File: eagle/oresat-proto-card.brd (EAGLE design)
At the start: 99.8 x 94.7 mm, 120 parts, among them J1 J-SAMTEC-TFM-110-X1-XXX-D-RA, J2 U.FL, J3 U.FL, J4 U.FL, J6 J-SAMTEC-TFM-120-X1-XXX-D-RA, J7 ORESAT-DEBUG-CONNECTOR-SOLAR, Q10 DMP2240UDM, Q2 MOSFET-PCH-SOT23-6, Q7 MOSFET-PCH-SOT23-6, Q8 PMV45EN, Q9 PMV45EN, U1 TCAN330, U10 TPS62111RSA, U11 MIC842LYC5, U12 MIC842LYC5, U2 MAX7310ATE, U6 MAX4211FETE, U7 STM32F091C, X2 16MHZ-2.5x2mm

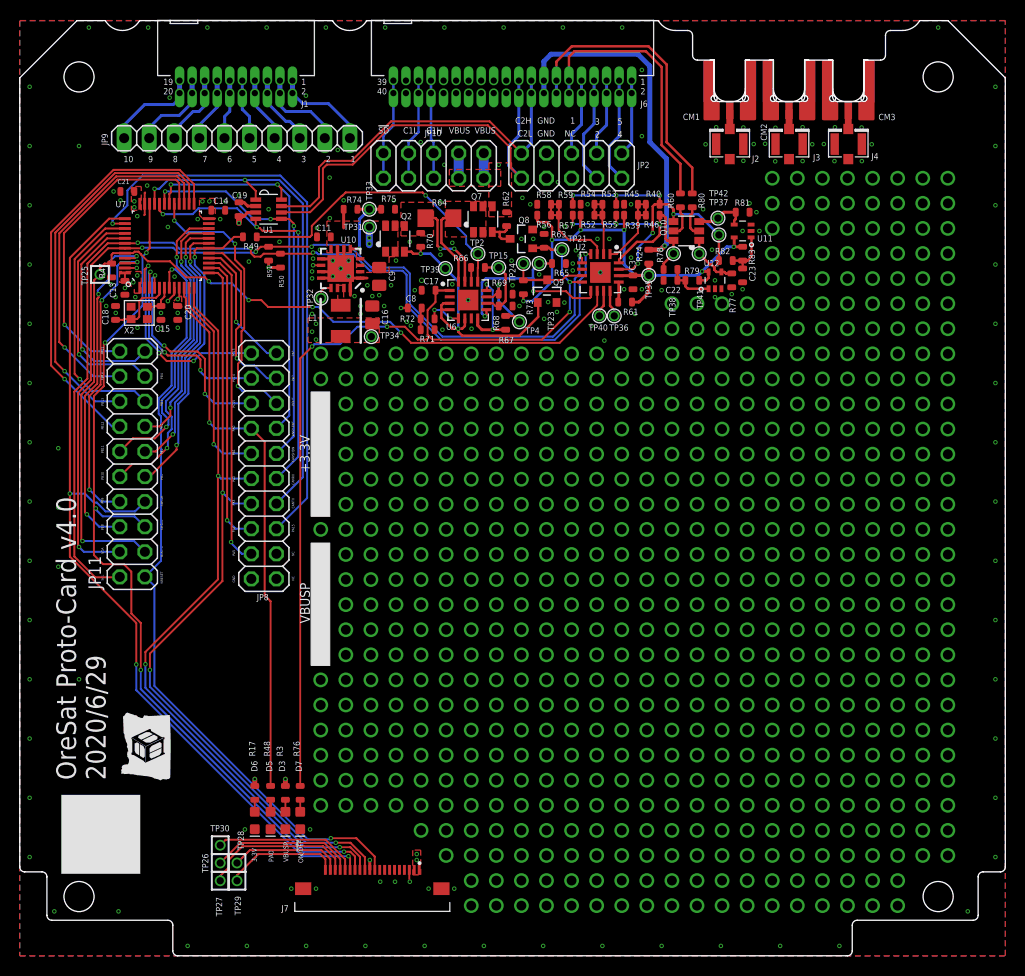
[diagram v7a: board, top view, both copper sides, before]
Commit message: Updated to 4.1: switched to better debug connector, fixed OPD capacitance problem.
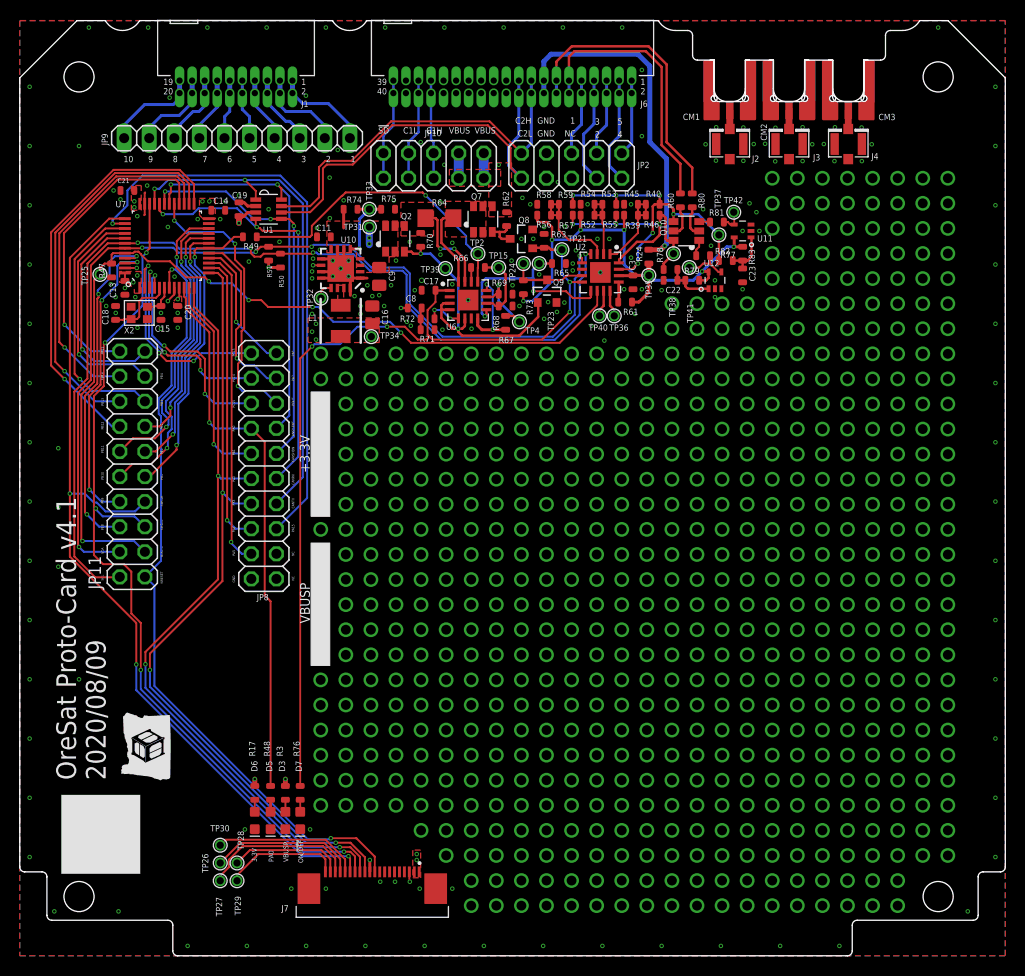
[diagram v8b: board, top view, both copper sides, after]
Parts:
- J7: value ORESAT-DEBUG-CONNECTOR-SOLAR -> ORESAT-DEBUG-CONNECTOR-ALL; device oresat-debug-connector:WURTH_687120183622 -> oresat-debug-connector:TE_2-1734592-0
- R77, R81: value 10k -> 665k
- TP25, TP26, TP27, TP28, TP29, TP30: value TEST-POINT -> TEST-POINT-LARGE-SQUARE; device Tova:2MM-TEST-POINT -> oresat-misc:1X01
- moved R77 3.83 mm to (69.2, 70.9), turned to 180 degrees
- moved R81 2.79 mm to (70.6, 74.3)
- moved TP41 1.72 mm to (67.8, 69.7)
- moved TP42 1.71 mm to (72.3, 75.3)
- moved C21 0.10 mm to (10.9, 77.5)
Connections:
- new net N$398: Q10.1, R77.2
- new net N$400: Q10.3, R81.2
- net GND: no longer R77.1, R81.1
- net N$539: now also R77.1; no longer Q10.1, R77.2
- net N$573: now also R81.1; no longer Q10.3, R81.2
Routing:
- net N$573: track 5.43 -> 2.42 mm
- net N$398: track 0.00 -> 1.67 mm
- net N$400: track 0.00 -> 1.12 mm
- net N$539: track 5.62 -> 4.57 mm
- net VBUSP: track 38.4 -> 37.8 mm
- net GND: track 24.1 -> 23.9 mm, vias 288 -> 287
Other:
- board text added: "2020/08/09"
- board text added: "OreSat Proto-Card v4.1"
- board text removed: "2020/6/29"
- board text removed: "OreSat Proto-Card v4.0"
